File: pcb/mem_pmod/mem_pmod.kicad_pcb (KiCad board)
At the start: 4 copper layers, 11 parts

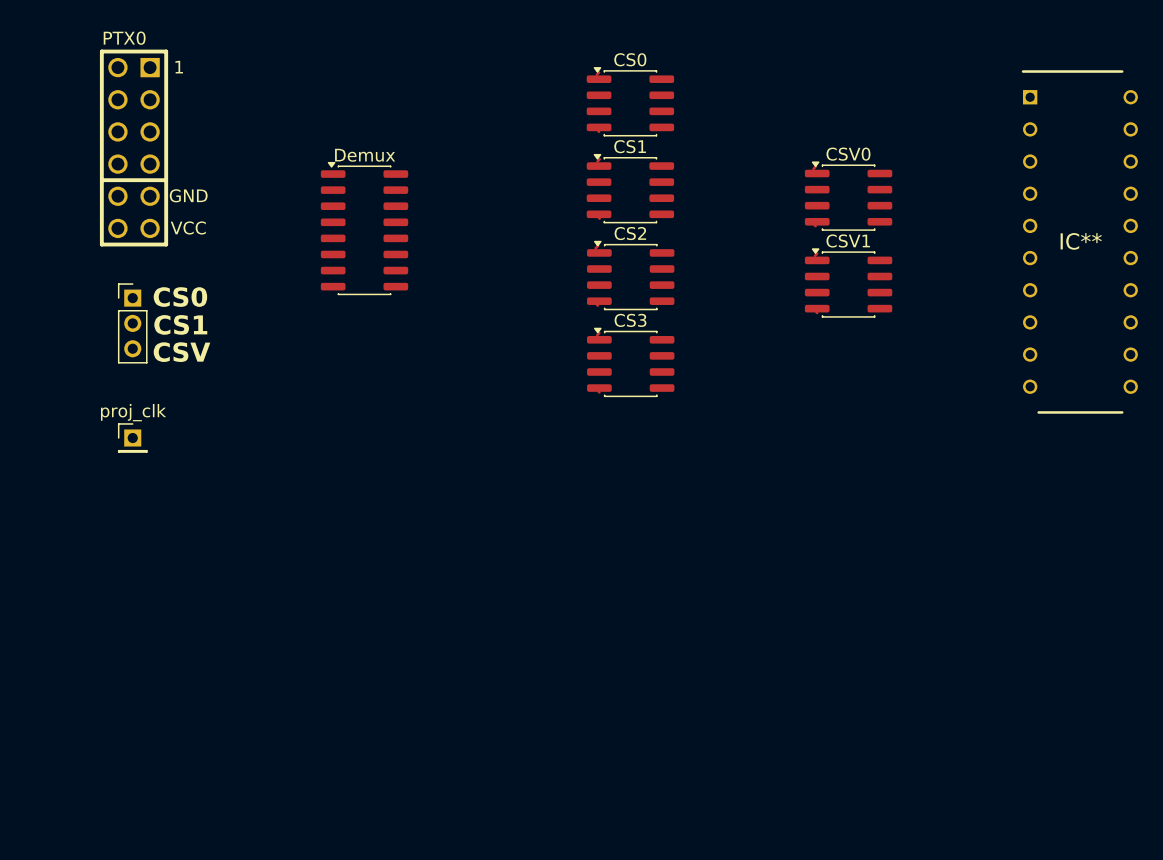
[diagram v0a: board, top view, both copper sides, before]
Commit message: more or less completed schematic. Still needs caps/resistors or whatever
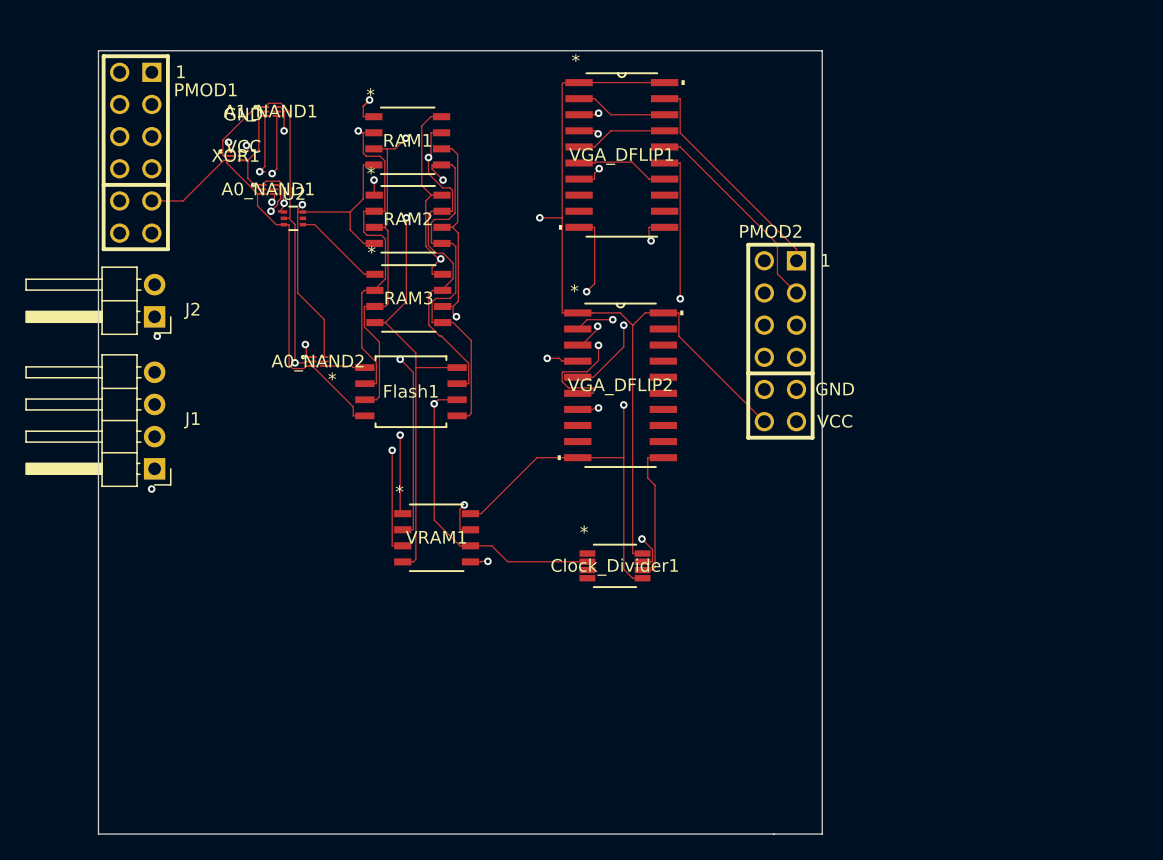
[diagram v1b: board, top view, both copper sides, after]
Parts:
- removed CS0, CS1, CS2, CS3, CSV0, CSV1: SOIC-8_3.9x4.9mm_P1.27mm, Package_SO:SOIC-8_3.9x4.9mm_P1.27mm
- removed Demux: SOIC-16_3.9x9.9mm_P1.27mm, footprints:SOIC-16_3.9x9.9mm_P1.27mm
- removed IC**: DIP794W53P254L2540H508Q20N, ff-dtype-TI-SN74HC273NE4:DIP794W53P254L2540H508Q20N
- removed PTX0: PMOD-CONN_6X2, pmod-conn_6x2:pmod_pin_array_6x2
- removed chip_sel: PinHeader_1x03_P2.00mm_Vertical, Connector_PinHeader_2.00mm:PinHeader_1x03_P2.00mm_Vertical
- removed proj_clk: PinHeader_1x01_P2.00mm_Vertical, Connector_PinHeader_2.00mm:PinHeader_1x01_P2.00mm_Vertical
- added A0_NAND1: NC7SZ86FHX, footprints:MICROPAK2-6_1X1_ONS, F.Cu at (25.6, 23.3)
- added A0_NAND2: NC7SZ86FHX, footprints:MICROPAK2-6_1X1_ONS, F.Cu at (29.6, 36.9)
- added A1_NAND1: NC7SZ86FHX, footprints:MICROPAK2-6_1X1_ONS, F.Cu at (25.8, 17.1)
- added Clock_Divider1: SY100EP32VKG, footprints:MSOP-8_K8-1_MCL, F.Cu at (53.0, 53.0)
- added Flash1: W25Q128JVSIM, footprints:SOIC_128JVSIM_WIN, F.Cu at (36.9, 39.2)
- added J1: Conn_01x04_Pin, Connector_PinHeader_2.54mm:PinHeader_1x04_P2.54mm_Horizontal, F.Cu at (16.6, 45.3)
- added J2: Conn_01x02_Pin, Connector_PinHeader_2.54mm:PinHeader_1x02_P2.54mm_Horizontal, F.Cu at (16.6, 33.3)
- added PMOD1: PMOD-Device-x2-Type-1A-GPIO, pmod-conn_6x2:pmod_pin_array_6x2, F.Cu at (15.1, 20.4)
- added PMOD2: PMOD-Device-x2-Type-1A-GPIO, pmod-conn_6x2:pmod_pin_array_6x2, F.Cu at (66.0, 35.3)
- added RAM1: APS6404L-3SQR-SN, footprints:APS6404L-3SQR-SN_APY, F.Cu at (36.6, 19.4)
- added RAM2: APS6404L-3SQR-SN, footprints:APS6404L-3SQR-SN_APY, F.Cu at (36.6, 25.6)
- added RAM3: APS6404L-3SQR-SN, footprints:APS6404L-3SQR-SN_APY, F.Cu at (36.7, 31.9)
- added U2: NL17SV32XV5T2G, footprints:SOT553-5_ONS, F.Cu at (27.6, 25.6)
- added VGA_DFLIP1: SN74HC374NSR, footprints:NS20, F.Cu at (53.5, 20.5)
- added VGA_DFLIP2: SN74HC374NSR, footprints:NS20, F.Cu at (53.4, 38.7)
- added VRAM1: APS6404L-3SQR-SN, footprints:APS6404L-3SQR-SN_APY, F.Cu at (38.9, 50.8)
- added XOR1: NC7SZ86FHX, footprints:MICROPAK2-6_1X1_ONS, F.Cu at (23.0, 20.6)
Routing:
- net VCC: track 0.00 -> 161.6 mm, vias 0 -> 6
- net GND: track 0.00 -> 121.4 mm, vias 0 -> 4
- net PMOD_A0: track 0.00 -> 57.5 mm, vias 0 -> 1
- net HSYNC: track 0.00 -> 51.3 mm
- net PMOD_B2: track 0.00 -> 49.2 mm, vias 0 -> 3
- net PRJ_Clock: track 0.00 -> 48.7 mm, vias 0 -> 2
- net PMOD_B0: track 0.00 -> 44.7 mm, vias 0 -> 3
- net PMOD_B3: track 0.00 -> 30.7 mm, vias 0 -> 2
- net CS_A1: track 0.00 -> 30.4 mm, vias 0 -> 1
- net PMOD_A1: track 0.00 -> 28.8 mm, vias 0 -> 1
- net PMOD_A3: track 0.00 -> 28.6 mm, vias 0 -> 1
- net CS_V0: track 0.00 -> 27.7 mm, vias 0 -> 1
- net PMOD_A2: track 0.00 -> 27.0 mm, vias 0 -> 1
- net VGA_B_0: track 0.00 -> 23.2 mm, vias 0 -> 1
- net PMOD_B1: track 0.00 -> 18.8 mm, vias 0 -> 4
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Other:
- board outline added: 57.1 x 61.8 mm
- board text removed: "CS0"
- board text removed: "CS1"
- board text removed: "CSV"
